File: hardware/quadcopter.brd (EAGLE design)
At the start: 130.1 x 130.1 mm, 91 parts, among them J1 HEADER-4POS-0.1IN-FEMALE-SMD-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, J2 HEADER-10POSTH-254X10, J3 HEADER-4POS-0.1IN-FEMALE, J4 AVR_SPI_PRG_6-SMD, M1 MOTOR_PADS_GND-MOLEX-SMD, M2 MOTOR_PADS_GND-MOLEX-SMD, M3 MOTOR_PADS_GND-MOLEX-SMD, M4 MOTOR_PADS_GND-MOLEX-SMD, P1 PROPELLOR-45MM, P2 PROPELLOR-45MM, P3 PROPELLOR-45MM, P4 PROPELLOR-45MM, Q1 N-MOSFET-SI2302DS, Q12 N-MOSFET-SI2302DS, Q2 N-MOSFET-SI2302DS, Q3 N-MOSFET-SI2302DS, Q4 N-MOSFET-SI2302DS, Q6 N-MOSFET-SI2302DS, Q8 N-MOSFET-SI2302DS, Q9 N-MOSFET-SI2302DS, SW1 PUSHBUTTON_-4.5X4.5, U1 ATMEGA128RFA1, U2 IMU_LSM9DS1-LSM9DS1, Y1 CRYSTAL5X3

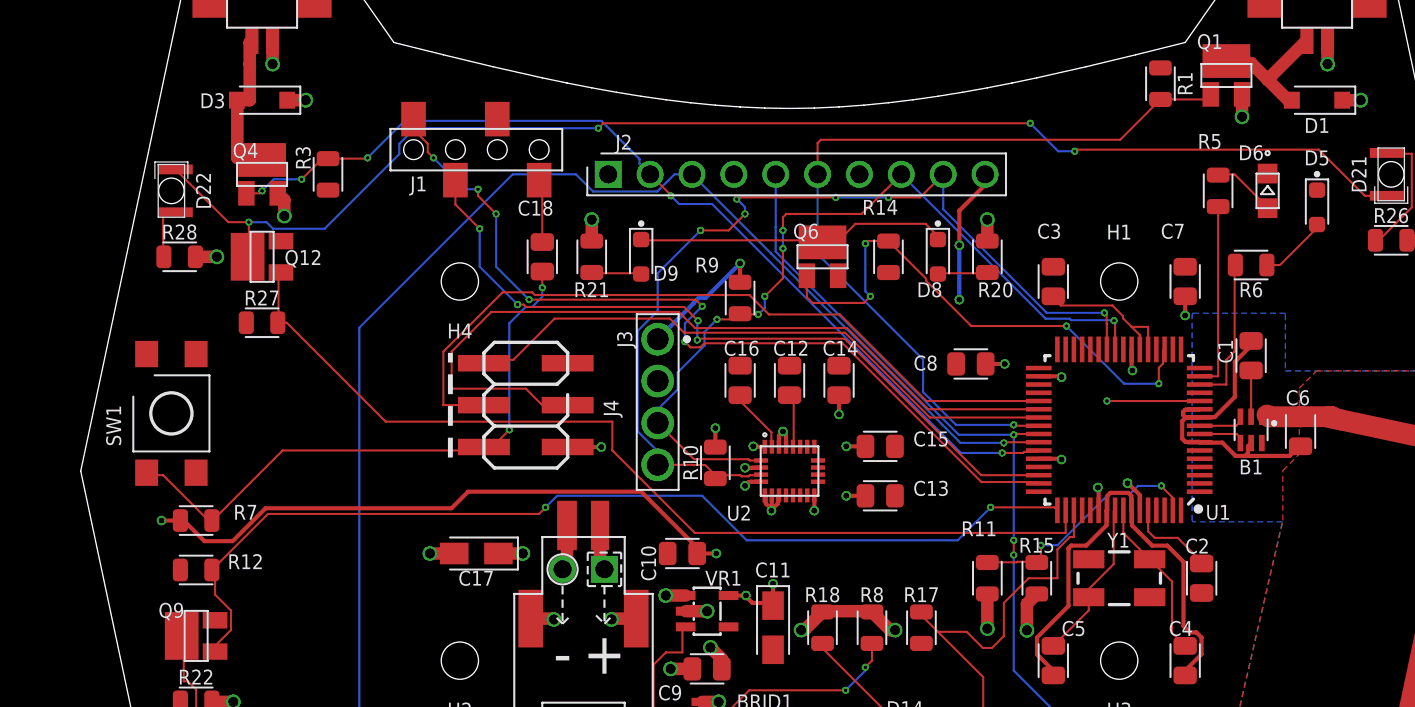
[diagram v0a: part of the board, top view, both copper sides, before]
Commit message: Implementing changes from design review
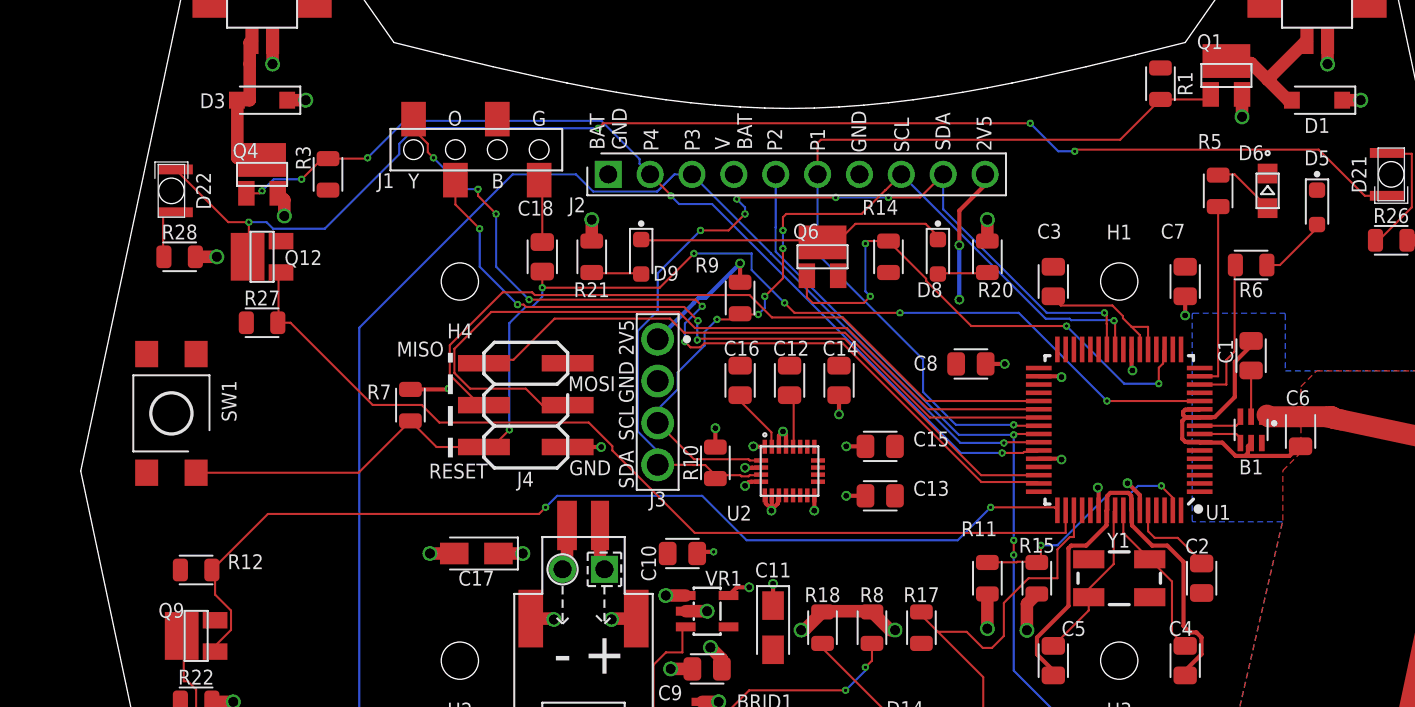
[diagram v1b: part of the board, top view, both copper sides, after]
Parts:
- moved R7 14.8 mm to (-23.0, 4.00), turned to 90 degrees
- turned SW1 to 90 degrees
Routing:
- net 2V5: track 81.4 -> 46.0 mm
- net RESET: track 79.5 -> 77.1 mm, vias 3 -> 6
- net SCK: track 46.0 -> 44.4 mm
- net PWM6: track 58.6 -> 57.8 mm
- net MOSI: track 48.8 -> 48.0 mm
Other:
- board text added: "2V5"
- board text added: "B"
- board text added: "BAT GND"
- board text added: "G"
- board text added: "GND"
- board text added: "MISO"
- board text added: "MOSI"
- board text added: "O"
- board text added: "P1"
- board text added: "P2"
- board text added: "P3"
- board text added: "P4"
- board text added: "RESET"
- board text added: "SCL"
- board text added: "SDA"
- board text added: "V BAT"
- board text added: "Y"

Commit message: Update LEDs to use latest lbr version
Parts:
- D15, D16, D21, D22: device LED:LED-350-2312-1-ND-REVERSE -> LED:1206_LED_REVERSE
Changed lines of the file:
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@@
 <attribute name="VALUE" x="7" y="-20.54" size="0.9" layer="27" font="vector" align="bottom-center"/>
 </element>
-<element name="D15" library="LED" library_urn="urn:adsk.wipprod:fs.file:vf.NaXM9vi8RxK1DTk1qfWV8Q" package="LED-350-2312-1-ND-REVERSE" value="red" x="-36.5" y="-18" smashed="yes" rot="R270">
+<element name="D15" library="LED" library_urn="urn:adsk.wipprod:fs.file:vf.NaXM9vi8RxK1DTk1qfWV8Q" package="1206_LED_REVERSE" value="red" x="-36.5" y="-18" smashed="yes" rot="R270">
 <attribute name="CREATOR" value="Evan Smith" x="-105.08" y="-82.77" size="1.778" layer="27" rot="R270" display="off"/>
 <attribute name="CUSTOM" value="" x="-105.08" y="-82.77" size="1.778" layer="27" rot="R270" display="off"/>
@@
 <attribute name="VALUE" x="-38" y="-18" size="0.9" layer="27" font="vector" rot="R270" align="top-center"/>
 </element>
-<element name="D16" library="LED" library_urn="urn:adsk.wipprod:fs.file:vf.NaXM9vi8RxK1DTk1qfWV8Q" package="LED-350-2312-1-ND-REVERSE" value="red" x="36.5" y="-23.5" smashed="yes" rot="R90">
+<element name="D16" library="LED" library_urn="urn:adsk.wipprod:fs.file:vf.NaXM9vi8RxK1DTk1qfWV8Q" package="1206_LED_REVERSE" value="red" x="36.5" y="-23.5" smashed="yes" rot="R90">
 <attribute name="CREATOR" value="Evan Smith" x="105.08" y="46.35" size="1.778" layer="27" rot="R90" display="off"/>
 <attribute name="CUSTOM" value="" x="105.08" y="46.35" size="1.778" layer="27" rot="R90" display="off"/>
@@
 <attribute name="REVIEWER" value="Swanson" x="112.09" y="45.58" size="1.778" layer="27" rot="R90" display="off"/>
 </element>
-<element name="D21" library="LED" library_urn="urn:adsk.wipprod:fs.file:vf.NaXM9vi8RxK1DTk1qfWV8Q" package="LED-350-2312-1-ND-REVERSE" value="red" x="36.5" y="18" smashed="yes" rot="R90">
+<element name="D21" library="LED" library_urn="urn:adsk.wipprod:fs.file:vf.NaXM9vi8RxK1DTk1qfWV8Q" package="1206_LED_REVERSE" value="red" x="36.5" y="18" smashed="yes" rot="R90">
 <attribute name="CREATOR" value="Evan Smith" x="105.08" y="92.93" size="1.778" layer="27" rot="R90" display="off"/>
 <attribute name="CUSTOM" value="" x="105.08" y="92.93" size="1.778" layer="27" rot="R90" display="off"/>
@@
 <attribute name="VALUE" x="37.9" y="17.8" size="0.9" layer="27" font="vector" rot="R90" align="top-center"/>
 </element>
-<element name="D22" library="LED" library_urn="urn:adsk.wipprod:fs.file:vf.NaXM9vi8RxK1DTk1qfWV8Q" package="LED-350-2312-1-ND-REVERSE" value="red" x="-37.5" y="17" smashed="yes" rot="R270">
+<element name="D22" library="LED" library_urn="urn:adsk.wipprod:fs.file:vf.NaXM9vi8RxK1DTk1qfWV8Q" package="1206_LED_REVERSE" value="red" x="-37.5" y="17" smashed="yes" rot="R270">
 <attribute name="CREATOR" value="Evan Smith" x="-112.43" y="1.76" size="1.778" layer="27" rot="R270" display="off"/>
 <attribute name="CUSTOM" value="" x="-112.43" y="1.76" size="1.778" layer="27" rot="R270" display="off"/>

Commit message: Add class logo, "created by" and date to the silkscreen
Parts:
- added DECO2: DECORATION-CLASS-LOGO-SMALL, quadparts_prebuilt_2022:QUADCLASS_LOGO_SMALL
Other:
- board text added: "Designed by: Michael Shao Evan Smith"
- board text added: "Rev 1 Feb. 2022"
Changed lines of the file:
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@@
 <setting verticaltext="up"/>
 </settings>
-<grid distance="0.1" unitdist="mm" unit="mm" style="lines" multiple="1" display="yes" altdistance="0.5" altunitdist="mm" altunit="mm"/>
+<grid distance="0.5" unitdist="mm" unit="mm" style="lines" multiple="1" display="yes" altdistance="0.5" altunitdist="mm" altunit="mm"/>
 <layers>
 <layer number="1" name="Top" color="4" fill="1" visible="yes" active="yes"/>
@@
 <text x="-9.9" y="8.1" size="0.9" layer="21" font="vector" rot="R90" align="center">2V5</text>
 <text x="-12" y="5.3" size="0.9" layer="21" font="vector" align="center">MOSI</text>
+<text x="-27.5" y="-3" size="0.9" layer="21" font="vector" rot="R270" align="center">Designed by:
+Michael Shao
+Evan Smith</text>
+<text x="11" y="-22.5" size="0.9" layer="21" font="vector">Rev 1
+Feb. 2022</text>
 </plain>
 <attributes>
@@
 <attribute name="DISTPN" value="NA" x="0" y="0" size="1.778" layer="27" display="off"/>
 </element>
+<element name="DECO2" library="quadparts_prebuilt_2022" library_urn="urn:adsk.wipprod:fs.file:vf.VudH_-qgS-enOFMGlZoxrw" package="QUADCLASS_LOGO_SMALL" value="DECORATION-CLASS-LOGO-SMALL" x="-27.5" y="-11" smashed="yes"/>
 </elements>
 <signals>
